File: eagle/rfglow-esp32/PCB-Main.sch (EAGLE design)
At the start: 27 parts, among them IC1 TLC59116PW, J1 4P-SMD-2.0-90D, J2 2P-2.0-90D-SMD, SW1 MK-12C02 G1.5, SW2 DHT-4235A, U1 XC6206P332MR-G-SOT23, U2 Value, X1 87438-06

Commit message: Consolidate libraries, swap regulator
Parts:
- removed C1: 100nf, Seeed-Capacitor:CERAMIC-100NF-25V-10%-X7R(0402)
- ANT1: device Seeed-Connector:ANTENNA-CONN-U-FL(3P) -> OPL_Connector:ANTENNA-CONN-U-FL(3P)
- C2, C3: device Seeed-Capacitor:CERAMIC-1UF-10V-10%-X5R(0402) -> OPL_Capacitor:CERAMIC-1UF-10V-10%-X5R(0402)
- J1: device Seeed-Connector:GROVE-CONNECTOR-SMD-90D(4+2P-2.0) -> OPL_Connector:GROVE-CONNECTOR-SMD-90D(4+2P-2.0)
- J2: device Seeed-Connector:CONN-HEADER-SMD-PH-SIDE-(2P-2.0MM) -> OPL_Connector:CONN-HEADER-SMD-PH-SIDE-(2P-2.0MM)
- R5: device Seeed-Resistor:SMD-RES-10K-1%-1/16W(0402) -> OPL_Resistor:SMD-RES-10K-1%-1/16W(0402)
- R6, R7: device Seeed-Resistor:SMD-RES-4.7K-5%-1/16W(0402) -> OPL_Resistor:SMD-RES-4.7K-5%-1/16W(0402)
- R8, R9: value 10M 1/16W -> 1M; device Seeed-Resistor:SMD-RES-10M-1%-1/16W(0402) -> OPL_Resistor:SMD-RES-1M-1%-1/16W(0402)
- SW1: device Seeed-Switch:SMD-TOGGLE-SWITCH-ON-ON(3+4P-6.7X2.7MM) -> OPL_Switch:SMD-TOGGLE-SWITCH-ON-ON(3+4P-6.7X2.7MM)
- SW2: device Seeed-Switch:SMD-BUTTON-TOP-DHT-4235A(4P-4.2X3.2MM) -> OPL_Switch:SMD-BUTTON-TOP-DHT-4235A(4P-4.2X3.2MM)
- U1: value XC6206P332MR-G-SOT23 -> AP2112K-3.3TRG1; device Seeed-IC:PMIC-LDO-XC6206P332MR-G(SOT23) -> rfglow-esp32:AP2112K-3.3TRG1
- U2: device Webench-Regulator:TPS63000DRCR -> Components:TPS63000DRCR
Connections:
- net GND: now also U1.GND; no longer C1.1, U1.VSS
- net N$17: no longer C1.2
- net V4.2: now also U1.EN
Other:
- moved on the sheet: C2, C3, C4, C5, C6, IC1, J2, R1, R10, R14, R15, R2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

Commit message: Removed unused parts for esp32, begin integrating actual module
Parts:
- removed ANT1: U-FL, OPL_Connector:ANTENNA-CONN-U-FL(3P)
- removed C6: 10uf, OPL_Capacitor:CERAMIC-10UF-6.3V-20%-X5R(0402)
- removed R14: 56R, OPL_Resistor:SMD-RES-56R-1%-1/10W(0603)
- removed U$1: PANSTAMP-AVR-2, Components:PANSTAMP-AVR-2
- removed X1: 87438-06, Components:87438-06
- added C1: 100uf, OPL_Capacitor:CERAMIC-100UF-6.3V-20%-X5R(1206)
- added IC4: ESP32-WROOM-32UNOSD, rfglow-esp32:ESP32-WROOM-32UNOSD
- added R3: 1M, OPL_Resistor:SMD-RES-1M-1%-1/16W(0402)
- added R4: 100K, OPL_Resistor:SMD-RES-100K-1%-1/16W(0402)
- C5: value 100uf -> 10uf; device OPL_Capacitor:CERAMIC-100UF-6.3V-20%-X5R(1206) -> OPL_Capacitor:CERAMIC-10UF-6.3V-20%-X5R(0402)
- R10: value 1M -> 56R; device OPL_Resistor:SMD-RES-1M-1%-1/16W(0402) -> OPL_Resistor:SMD-RES-56R-1%-1/10W(0603)
- SW2: value DHT-4235A -> SKRPABE010; device OPL_Switch:SMD-BUTTON-TOP-DHT-4235A(4P-4.2X3.2MM) -> rfglow-esp32:SKRPABE010
- renumbered R15 to R11, U$2 to L1, U1 to IC3, U2 to IC2
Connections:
- removed net ANT: ANT1.D, U$1.31-ANT
- removed net AREF: U$1.11-AREF, X1-2.S
- removed net N$17: R8.1, R9.2, U$1.10-D8/A0-PC0
- removed net RST: U$1.12-RST, X1-6.S
- removed net RXD: U$1.17-D5-RXD, X1-5.S
- removed net TXD: U$1.16-D6-TXD, X1-4.S
- new net BATSENSE: R8.1, R9.2
- new net N$4: IC3.EN, R4.1
- net BUTTON: now also SW2.4; no longer SW2.B1, U$1.27-D18(PWM)-INT1
- net GND: now also C1.1, R10.1, SW2.1; no longer ANT1.GND1, ANT1.GND2, C6.1, R14.1, SW2.A0, U$1.14-GND, U$1.30-GND, U$1.32-GND, X1-1.S
- net I2CSCL: no longer U$1.18-D4/A5-SCL
- net I2CSDA: no longer U$1.19-D3/A4-SDA
- net N$3: now also R3.1; no longer R10.1
- net N$5: now also R10.2; no longer R14.2
- net V3.3: no longer U$1.13-VCC, X1-3.S
- net V4.2: now also C1.2, R3.2, R4.2; no longer C5.2, IC3.EN, R10.2
- net VBAT: now also C5.2; no longer C6.2
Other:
- moved on the sheet: C3, C5, R10, R6, R7, R8, R9

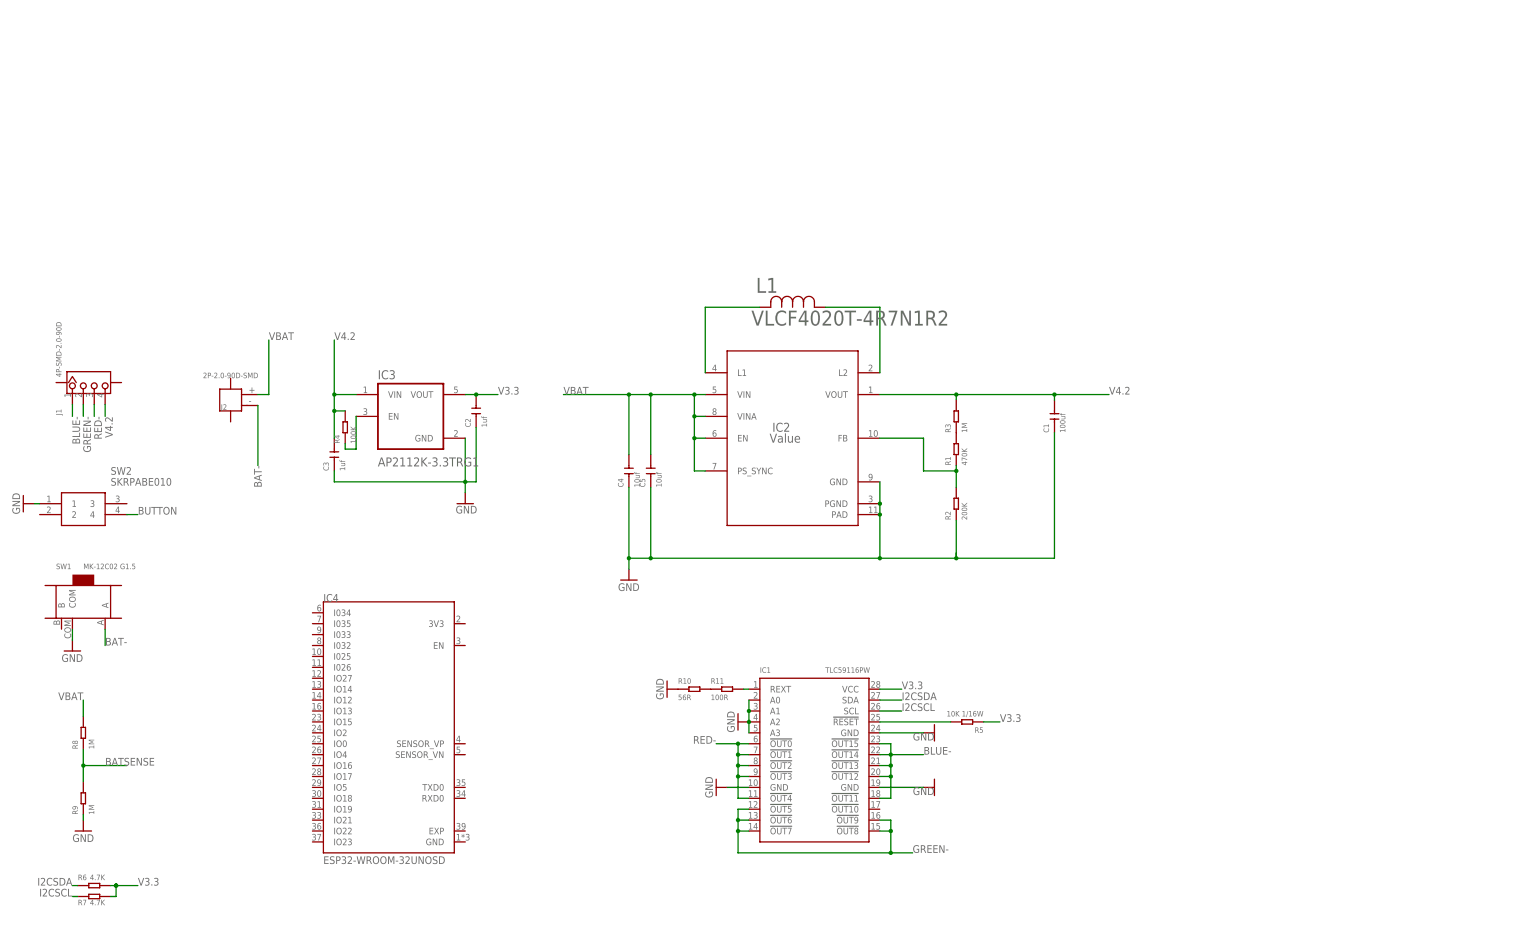
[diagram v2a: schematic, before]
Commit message: Board layout with UART but without LIPO charger, submitted this one to PCBA
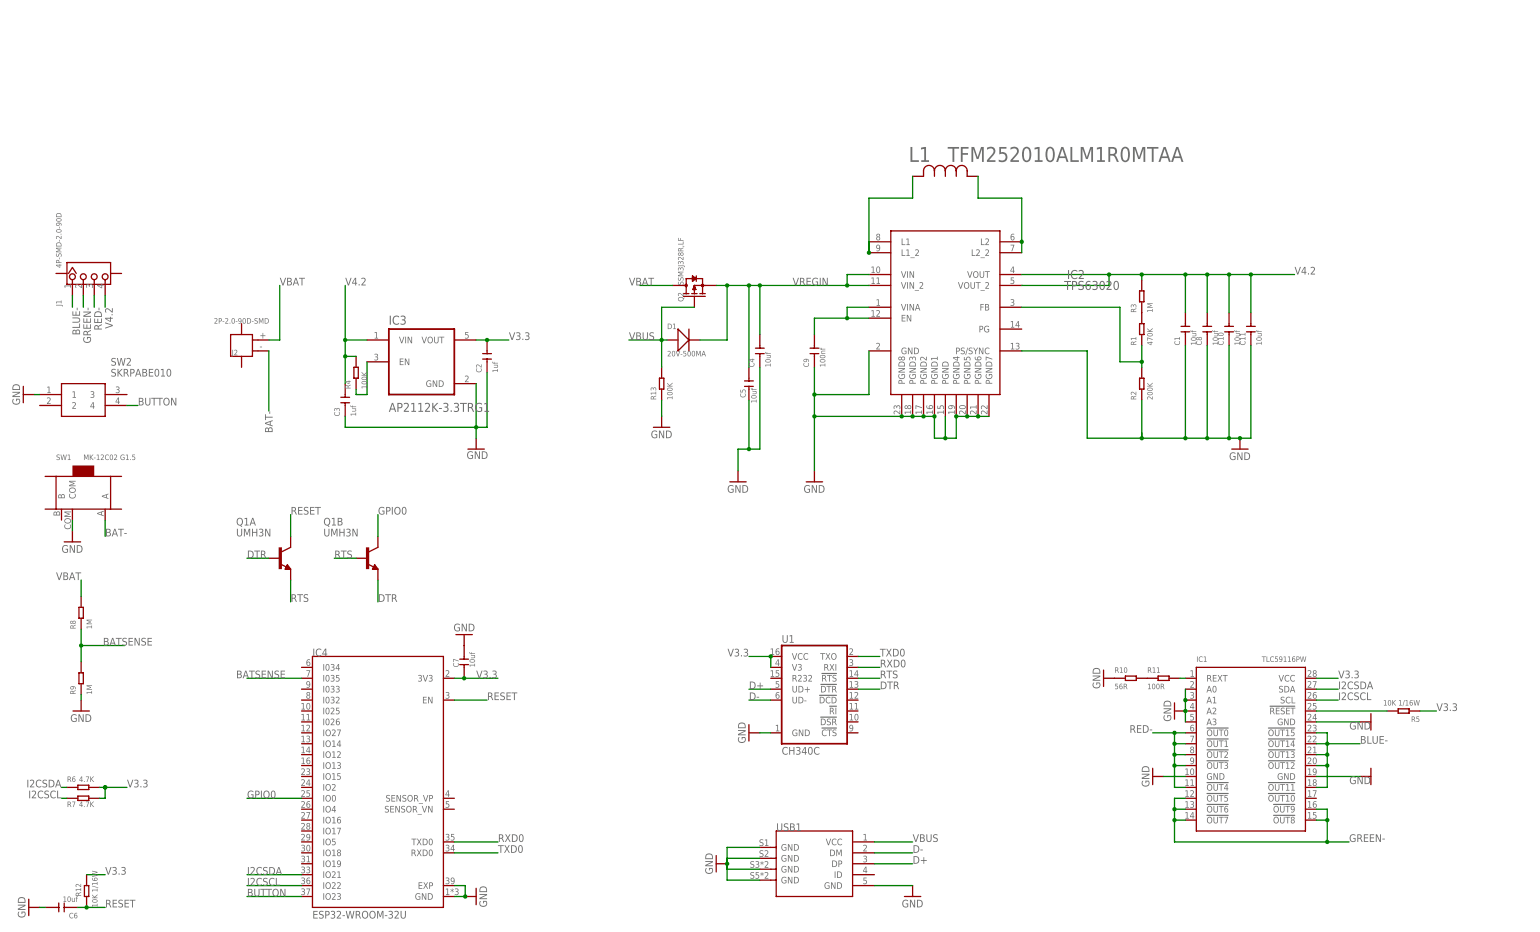
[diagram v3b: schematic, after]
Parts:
- added C10, C11, C6, C7, C8: 10uf, OPL_Capacitor:CERAMIC-10UF-6.3V-20%-X5R(0402)
- added C9: 100nf, OPL_Capacitor:CERAMIC-100NF-25V-10%-X7R(0402)
- added D1: 20V-500MA, OPL_Discrete_Semiconductor:SMD-DIODE-SCHOTTKY-20V-500MA(SOD-123)
- added Q1: UMH3N, rfglow-esp32:UMH3N
- added Q2: SSM3J328R,LF, OPL_Discrete_Semiconductor:SMD-MOSFET-P-CH-20V-6A-SSM3J328R(SOT-23)
- added R12: 10K 1/16W, OPL_Resistor:SMD-RES-10K-1%-1/16W(0402)
- added R13: 100K, OPL_Resistor:SMD-RES-100K-1%-1/16W(0402)
- added U1: CH340C, rfglow-esp32:CH340C
- added USB1: 10118193-0001LF, OPL_Connector:MICRO-USB-SMD-B-(10118193-0001LF)
- C1: value 100uf -> 10uf; device OPL_Capacitor:CERAMIC-100UF-6.3V-20%-X5R(1206) -> OPL_Capacitor:CERAMIC-10UF-6.3V-20%-X5R(0402)
- IC1: device Components:TLC59116PW -> rfglow-esp32:TLC59116PW
- IC2: value Value -> TPS63020; device Components:TPS63000DRCR -> rfglow-esp32:TPS63020
- IC4: value ESP32-WROOM-32UNOSD -> ESP32-WROOM-32U
- L1: value VLCF4020T-4R7N1R2 -> TFM252010ALM1R0MTAA; device Components:VLCF4020T-4R7N1R2 -> rfglow-esp32:TFM252010ALM1R0MTAA
- R10: device OPL_Resistor:SMD-RES-56R-1%-1/10W(0603) -> rfglow-esp32:SMD-RES-56Ω-1%-1/16W(0402)
- R11: device OPL_Resistor:SMD-RES-100R-5%-1/16W(0402) -> rfglow-esp32:SMD-RES-100R-5%-1/16W(0402)
- R3, R8, R9: device OPL_Resistor:SMD-RES-1M-1%-1/16W(0402) -> rfglow-esp32:SMD-RES-1M-1%-1/16W(0402)
- R6, R7: device OPL_Resistor:SMD-RES-4.7K-5%-1/16W(0402) -> rfglow-esp32:SMD-RES-4.7K-5%-1/16W(0402)
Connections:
- new net D+: U1.UD+, USB1.DP
- new net D-: U1.UD-, USB1.DM
- new net DTR: Q1A.B, Q1B.E, U1.!DTR
- new net GPIO0: IC4.IO0, Q1B.C
- new net N$8: IC2.L2, IC2.L2_2, L1.1
- new net RESET: C6.1, IC4.EN, Q1A.C, R12.1
- new net RTS: Q1A.E, Q1B.B, U1.!RTS
- new net RXD0: IC4.TXD0, U1.RXI
- new net TXD0: IC4.RXD0, U1.TXO
- new net VBUS: D1.+, Q2.G, R13.2, USB1.VCC
- new net VREGIN: C4.2, C5.2, D1.-, IC2.VIN, IC2.VIN_2, Q2.S
- net BATSENSE: now also IC4.I035
- net BUTTON: now also IC4.IO23
- net GND: now also C10.1, C11.1, C6.2, C7.2, C8.1, C9.1, IC2.PGND1, IC2.PGND2, IC2.PGND3, IC2.PGND4, IC2.PGND5, IC2.PGND6, IC2.PGND7, IC2.PGND8, IC2.PS/SYNC, IC4.EXP, IC4.GND, R13.1, U1.GND, USB1.GND@1, USB1.GND@2, USB1.GND@3, USB1.GND@4, USB1.GND@5; no longer IC2.PAD
- net I2CSCL: now also IC4.IO22
- net I2CSDA: now also IC4.IO21
- net N$1: now also C9.2, IC2.EN, IC2.VINA; no longer IC2.L1, L1.2
- net N$6: now also IC2.L1, IC2.L1_2, L1.2; no longer IC2.L2, L1.1
- net V3.3: now also C7.1, IC4.3V3, R12.2, U1.V3, U1.VCC
- net V4.2: now also C10.2, C11.2, C8.2, IC2.VOUT_2
- net VBAT: now also Q2.D; no longer C4.2, C5.2, IC2.EN, IC2.PS_SYNC, IC2.VIN, IC2.VINA
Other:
- moved on the sheet: C1, C2, C3, C4, C5, IC1, IC3, IC4, J1, J2, L1, R1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
